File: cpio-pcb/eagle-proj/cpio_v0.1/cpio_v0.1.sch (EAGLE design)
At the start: 96 parts

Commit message: Schematic completed with GPIOS
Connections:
- net N$23 renamed GPIO13
- net N$36 renamed GPIO19
- net N$37 renamed GPIO26
- net N$60 renamed GPIO22
- net N$62 renamed GPIO5
- net N$63 renamed GPIO6
- net N$65 renamed GPIO17
- net N$66 renamed GPIO27
- removed net N$38: R_HSS_PROT_3.1
- removed net N$39: R_SS_PROT0.1
- removed net N$40: R_SS_PROT1.1
- removed net N$41: R_SS_PROT2.1
- removed net N$42: R_SS_PROT3.1
- net 3.3V: now also C_LDO3.3_2.1
- net 5V: now also C_LDO3.3_1.1
- net GPIO12: now also R_SS_PROT2.1
- net GPIO16: now also R_SS_PROT1.1
- net GPIO20: now also R_SS_PROT0.1
- net GPIO21: now also R_HSS_PROT_3.1
- net GPIO25: now also R_SS_PROT3.1
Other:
- note removed: "To which GPIOs?!"
- moved on the sheet: ADC, BEEP, CAMERA, C_ADC, C_LDO3.3_1, C_LDO3.3_2, C_RL_0, C_RL_1, C_RL_10, C_RL_11, C_RL_2, C_RL_3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

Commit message: First Review and modification of schematic
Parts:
- removed R_RGBLED: (no value), SparkFun-Passives:RESISTOR0805-RES
- removed R_SD_1A: 20k, SparkFun-Passives:RESISTOR0805-RES
- removed R_SD_2B: 9.1k, SparkFun-Passives:RESISTOR0805-RES
- removed R_SPI_0, R_SPI_1, R_SPI_2: 10k, SparkFun-Passives:RESISTOR0805-RES
- added C_ADC_B, C_ADC_PH, C_CUR_FILT, C_LVL, C_MUX, C_RL_12, C_SW, C_U_FILT: 100n, SparkFun-Passives:CAP0805
- added PUSH1: BUTTON, cpio:BUTTON
- added R_CM_LOAD1, R_CM_LOAD2: 100, SparkFun-Passives:RESISTOR0805-RES
- added R_PH: 10k, SparkFun-Passives:RESISTOR0805-RES
- added R_PUSHBUT1, R_PUSHBUT2: (no value), SparkFun-Passives:RESISTOR0805-RES
- added SENS_PH: XH-A-3, cpio:XH-A-3
- added U$2: DB2X41100L, cpio:DB2X41100L
- C_SD_3: value (none) -> 10n
- R_SD_1B: value 30k -> 82k
- R_SD_2A: value 430 -> 15k
- R_SD_EN: value 10M -> 10k
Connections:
- net GPIO27 renamed GPIO_XXXXX
- removed net ADC_PWR: ADC.AIN0, R_CM_LOAD.2, SENS_I.OUT
- removed net N$52: C_RL_10.1, C_RL_11.1, C_RL_8.1, C_RL_9.1, RL_BRIGHT.VDD, RL_CAMERA.VDD, RL_HUM_0.VDD, RL_HUM_1.VDD, R_RGBLED.1
- removed net N$61: C_RL_4.1, C_RL_5.1, C_RL_6.1, C_RL_7.1, RL_TEMP_0.VDD, RL_TEMP_1.VDD, RL_TEMP_2.VDD, RL_TEMP_3.VDD
- removed net N$67: C_RL_0.1, C_RL_1.1, C_RL_2.1, C_RL_3.1, RL_HEAT_0.VDD, RL_HEAT_1.VDD, RL_HEAT_2.VDD, RL_HEAT_3.VDD
- new net 3.3V1: C_MUX.2
- new net 3.3V2: C_SW.2
- new net 3.3V3: C_LVL.2
- new net ADC_CUR: ADC.AIN0, C_CUR_FILT.1, R_CM_LOAD.2, SENS_I.OUT
- new net ADC_PH: ADC.AIN3, C_ADC_PH.1, R_PH.1
- new net ADC_U: ADC.AIN1, C_U_FILT.1, R_CM_LOAD1.1, R_CM_LOAD2.2
- new net N$23: SWT_PWR.3, U$2.A
- new net N$7: R_PH.2, SENS_PH.1
- new net PI_3.3V: RP_HEAD.1, RP_HEAD.17
- net 12V: now also R_CM_LOAD1.2
- net 3.3V: now also R_PUSHBUT1.2; no longer RP_HEAD.1, RP_HEAD.17, R_SPI_0.2, R_SPI_1.2, R_SPI_2.2
- net 5V: now also C_RL_0.1, C_RL_1.1, C_RL_10.1, C_RL_11.1, C_RL_2.1, C_RL_3.1, C_RL_4.1, C_RL_5.1, C_RL_6.1, C_RL_7.1, C_RL_8.1, C_RL_9.1, RL_BRIGHT.VDD, RL_CAMERA.VDD, RL_HEAT_0.VDD, RL_HEAT_1.VDD, RL_HEAT_2.VDD, RL_HEAT_3.VDD, RL_HUM_0.VDD, RL_HUM_1.VDD, RL_TEMP_0.VDD, RL_TEMP_1.VDD, RL_TEMP_2.VDD, RL_TEMP_3.VDD; no longer R_RGBLED.2
- net ADC_BRIGHT: now also ADC.AIN2, C_ADC_B.1; no longer ADC.AIN1
- net GND: now also C_ADC_B.2, C_ADC_PH.2, C_LVL.1, C_MUX.1, C_RL_12.2, C_SW.1, C_U_FILT.2, PUSH1.P$1, R_CM_LOAD2.1
- net N$12: no longer R_SD_1A.1, R_SD_2B.2
- net N$13: no longer R_SD_2B.1
- net N$24: now also R_CM_SENS.1, SENS_I.VIN+, U$2.C; no longer ADC.AIN2
- net N$25: now also C_RL_12.1, R_PUSHBUT2.1; no longer ADC.AIN3
- net N$5: now also PUSH1.P$2, R_PUSHBUT1.1, R_PUSHBUT2.2; no longer R_CM_SENS.1, SENS_I.VIN+, SWT_PWR.3
- net N$9: no longer R_SD_1A.2
- net SPI0_MISO: no longer R_SPI_1.1
- net SPI0_MOSI: no longer R_SPI_2.1
- net SPI0_SCLK: no longer R_SPI_0.1
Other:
- note added: "1.2A"
- note added: "300mA"
- note added: "5.17V"
- note added: "5V is used for supply of Pi only: Pi should have an internal supply for 3.3V etc."
- note added: "Check Circuit!!!!"
- note added: "Check Suitability of Diode"
- note added: "Comments Raffael -Removed PullUps from SPI -simpler resisitive divider for 5V supply. Precision is not required. -Added some decoupling caps -Removed R for RGB. connected the three supply nets to 5V -Disconnected Pi's 3.3V from our 3.3V -Added protection Diode at supply input. -> now we can remove the ground protection circuit of the switch IC -Maybe overkill to have cap for each led. Can put foo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"
- note added: "Pull UP Required?"
- note removed: "DeCap?!"
- note removed: "Plugs for potential pH Sensors missing!"
- moved on the sheet: C_SD_1, C_SD_2, LED_PWR_12V, PUSH, R_LED_12V, R_PUSHBUT, R_SD_2A, R_SD_EN, STP_DN, SWT_PWR

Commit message: schematic review: button and some R less
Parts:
- removed C_RL_1, C_RL_11, C_RL_3, C_RL_5, C_RL_7, C_RL_9: 100n, SparkFun-Passives:CAP0805
- removed PUSH: BUTTON, cpio:BUTTON
- removed R_PUSHBUT: (no value), SparkFun-Passives:RESISTOR0805-RES
- removed R_SS_PROT0, R_SS_PROT1, R_SS_PROT2, R_SS_PROT3: 1k, SparkFun-Passives:RESISTOR0805-RES
- removed SENS_BRIGHT: XH-A-2, cpio:XH-A-2
- added C_IO1: 100n, SparkFun-Passives:CAP0805
- added SENS_PH1: XH-A-3, cpio:XH-A-3
- renumbered R_LED_3.3V1 to R_BEP
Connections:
- removed net GPIO_XXXXX: PUSH.P$1
- removed net N$20: R_SS_PROT1.2, SWT_SENS.2OE
- removed net N$21: R_SS_PROT2.2, SWT_SENS.3OE
- removed net N$22: R_SS_PROT3.2, SWT_SENS.4OE
- removed net N$25: C_RL_12.1, R_PUSHBUT2.1
- removed net N$57: PUSH.P$2, R_PUSHBUT.1
- new net GPIO_27: C_RL_12.1, R_PUSHBUT1.1, R_PUSHBUT2.2
- net 3.3V: now also C_IO1.1, SENS_PH.1, SENS_PH1.1; no longer R_PUSHBUT.2
- net 5V: no longer C_RL_1.1, C_RL_11.1, C_RL_3.1, C_RL_5.1, C_RL_7.1, C_RL_9.1
- net GND: now also C_IO1.2, SENS_PH.3, SENS_PH1.3; no longer C_RL_1.2, C_RL_11.2, C_RL_3.2, C_RL_5.2, C_RL_7.2, C_RL_9.2, SENS_BRIGHT.2
- net GPIO12: now also SWT_SENS.3OE; no longer R_SS_PROT2.1
- net GPIO16: now also SWT_SENS.2OE; no longer R_SS_PROT1.1
- net GPIO20: now also SWT_SENS.1OE; no longer R_SS_PROT0.1
- net GPIO25: now also SWT_SENS.4OE; no longer R_SS_PROT3.1
- net N$14: now also RL_HUM_0.DI; no longer R_SS_PROT0.2, SWT_SENS.1OE
- net N$35: now also SENS_PH1.2; no longer SENS_BRIGHT.1
- net N$5: now also R_PUSHBUT2.1; no longer R_PUSHBUT1.1, R_PUSHBUT2.2
- net N$58: no longer RL_HUM_0.DI
- net N$7: now also SENS_PH.2; no longer SENS_PH.1
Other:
- note added: "Comments Raffael -Removed PullUps from SPI -simpler resisitive divider for 5V supply. Precision is not required. -Added some decoupling caps -Removed R for RGB. connected the three supply nets to 5V -Disconnected Pi's 3.3V from our 3.3V -Added protection Diode at supply input. -> now we can remove the ground protection circuit of the switch IC -Values of current measurement need to be adapted. Wh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"
- note removed: "Check Circuit!!!!"
- note removed: "Comments Raffael -Removed PullUps from SPI -simpler resisitive divider for 5V supply. Precision is not required. -Added some decoupling caps -Removed R for RGB. connected the three supply nets to 5V -Disconnected Pi's 3.3V from our 3.3V -Added protection Diode at supply input. -> now we can remove the ground protection circuit of the switch IC -Maybe overkill to have cap for each led. Can put foo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"
- moved on the sheet: C_ADC_B, C_RL_12, PUSH1, R_BRIGHT, R_PUSHBUT1, R_PUSHBUT2, SENS_PH

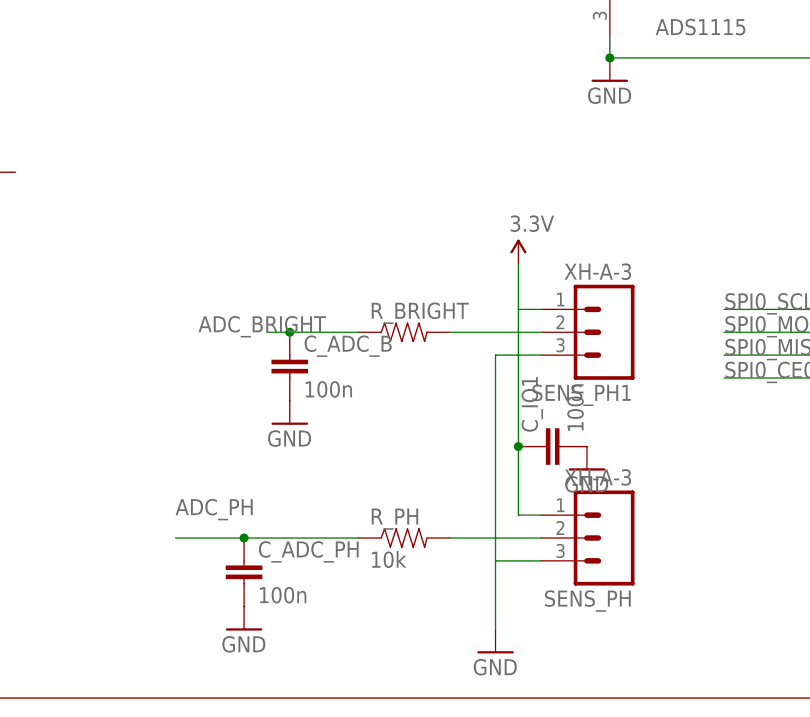
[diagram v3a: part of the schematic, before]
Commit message: rename brightness input. Now with gnd, signal, vcc
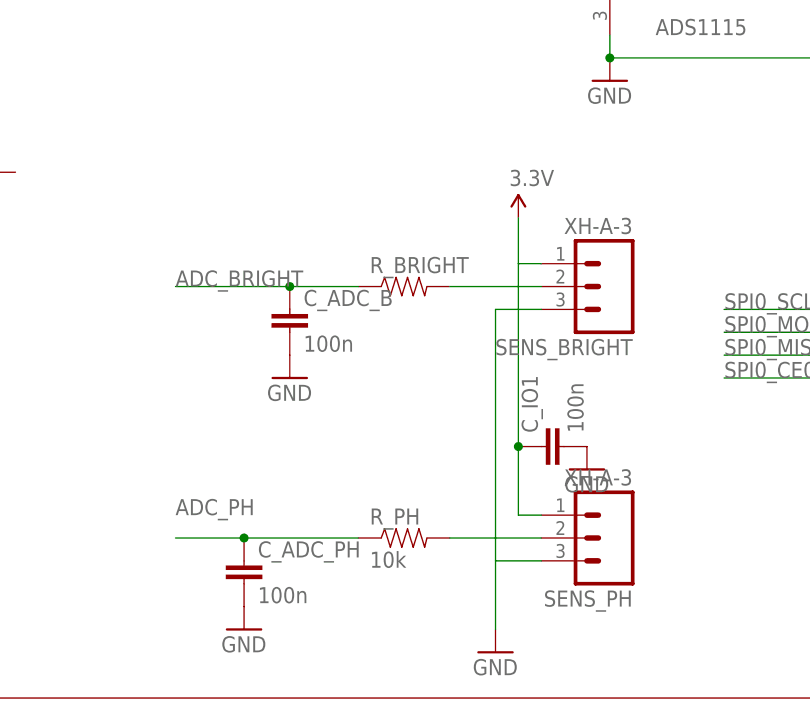
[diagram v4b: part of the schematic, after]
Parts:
- removed SENS_PH1: XH-A-3, cpio:XH-A-3
- added SENS_BRIGHT: XH-A-3, cpio:XH-A-3
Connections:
- net 3.3V: now also SENS_BRIGHT.1; no longer SENS_PH1.1
- net GND: now also SENS_BRIGHT.3; no longer SENS_PH1.3
- net N$35: now also SENS_BRIGHT.2; no longer SENS_PH1.2
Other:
- moved on the sheet: C_ADC_B, R_BRIGHT
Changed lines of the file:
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@@
 <part name="GND52" library="supply1" deviceset="GND" device=""/>
 <part name="SUPPLY7" library="SparkFun-Aesthetics" deviceset="3.3V" device=""/>
-<part name="SENS_PH1" library="cpio" deviceset="XH-A-3" device=""/>
+<part name="SENS_BRIGHT" library="cpio" deviceset="XH-A-3" device=""/>
 <part name="SUPPLY25" library="SparkFun-Aesthetics" deviceset="3.3V" device=""/>
 <part name="C_IO1" library="SparkFun-Passives" deviceset="CAP" device="0805" value="100n"/>
@@
 <instance part="R_HSS_PROT_3" gate="G$1" x="355.6" y="-30.48"/>
 <instance part="GND27" gate="1" x="355.6" y="-254"/>
-<instance part="R_BRIGHT" gate="G$1" x="345.44" y="-218.44"/>
+<instance part="R_BRIGHT" gate="G$1" x="345.44" y="-213.36"/>
 <instance part="CAMERA" gate="G$1" x="401.32" y="-218.44" rot="R180"/>
 <instance part="GND28" gate="1" x="393.7" y="-233.68"/>
@@
 <instance part="GND48" gate="1" x="251.46" y="-38.1"/>
 <instance part="SENS_PH" gate="G$1" x="368.3" y="-241.3" rot="R180"/>
-<instance part="C_ADC_B" gate="G$1" x="332.74" y="-223.52"/>
-<instance part="GND49" gate="1" x="332.74" y="-228.6"/>
+<instance part="C_ADC_B" gate="G$1" x="332.74" y="-218.44"/>
+<instance part="GND49" gate="1" x="332.74" y="-223.52"/>
 <instance part="GND50" gate="1" x="327.66" y="-251.46"/>
 <instance part="C_ADC_PH" gate="G$1" x="327.66" y="-246.38"/>
@@
 <instance part="GND52" gate="1" x="172.72" y="-251.46"/>
 <instance part="SUPPLY7" gate="G$1" x="172.72" y="-218.44"/>
-<instance part="SENS_PH1" gate="G$1" x="368.3" y="-218.44" rot="R180"/>
-<instance part="SUPPLY25" gate="G$1" x="358.14" y="-210.82"/>
+<instance part="SENS_BRIGHT" gate="G$1" x="368.3" y="-213.36" rot="R180"/>
+<instance part="SUPPLY25" gate="G$1" x="358.14" y="-205.74"/>
 <instance part="C_IO1" gate="G$1" x="363.22" y="-231.14" rot="R90"/>
 <instance part="GND53" gate="1" x="365.76" y="-233.68"/>
@@
 </segment>
 <segment>
-<wire x1="360.68" y1="-220.98" x2="355.6" y2="-220.98" width="0.1524" layer="91"/>
-<wire x1="355.6" y1="-220.98" x2="355.6" y2="-243.84" width="0.1524" layer="91"/>
+<wire x1="360.68" y1="-215.9" x2="355.6" y2="-215.9" width="0.1524" layer="91"/>
+<wire x1="355.6" y1="-215.9" x2="355.6" y2="-243.84" width="0.1524" layer="91"/>
 <pinref part="GND27" gate="1" pin="GND"/>
-<pinref part="SENS_PH1" gate="G$1" pin="3"/>
+<pinref part="SENS_BRIGHT" gate="G$1" pin="3"/>
 <pinref part="SENS_PH" gate="G$1" pin="3"/>
 <wire x1="355.6" y1="-243.84" x2="355.6" y2="-251.46" width="0.1524" layer="91"/>
@@
 <wire x1="360.68" y1="-238.76" x2="358.14" y2="-238.76" width="0.1524" layer="91"/>
 <wire x1="358.14" y1="-238.76" x2="358.14" y2="-231.14" width="0.1524" layer="91"/>
-<pinref part="SENS_PH1" gate="G$1" pin="1"/>
-<wire x1="358.14" y1="-231.14" x2="358.14" y2="-215.9" width="0.1524" layer="91"/>
-<wire x1="358.14" y1="-215.9" x2="358.14" y2="-210.82" width="0.1524" layer="91"/>
-<wire x1="360.68" y1="-215.9" x2="358.14" y2="-215.9" width="0.1524" layer="91"/>
+<pinref part="SENS_BRIGHT" gate="G$1" pin="1"/>
+<wire x1="358.14" y1="-231.14" x2="358.14" y2="-210.82" width="0.1524" layer="91"/>
+<wire x1="358.14" y1="-210.82" x2="358.14" y2="-205.74" width="0.1524" layer="91"/>
+<wire x1="360.68" y1="-210.82" x2="358.14" y2="-210.82" width="0.1524" layer="91"/>
 <pinref part="SUPPLY25" gate="G$1" pin="3.3V"/>
 <pinref part="C_IO1" gate="G$1" pin="1"/>
@@
 <segment>
 <pinref part="R_BRIGHT" gate="G$1" pin="2"/>
-<wire x1="360.68" y1="-218.44" x2="350.52" y2="-218.44" width="0.1524" layer="91"/>
-<pinref part="SENS_PH1" gate="G$1" pin="2"/>
+<wire x1="360.68" y1="-213.36" x2="350.52" y2="-213.36" width="0.1524" layer="91"/>
+<pinref part="SENS_BRIGHT" gate="G$1" pin="2"/>
 </segment>
 </net>
@@
 <segment>
 <pinref part="R_BRIGHT" gate="G$1" pin="1"/>
-<wire x1="340.36" y1="-218.44" x2="332.74" y2="-218.44" width="0.1524" layer="91"/>
-<label x="322.58" y="-218.44" size="1.778" layer="95"/>
+<wire x1="340.36" y1="-213.36" x2="332.74" y2="-213.36" width="0.1524" layer="91"/>
+<label x="320.04" y="-213.36" size="1.778" layer="95"/>
 <pinref part="C_ADC_B" gate="G$1" pin="1"/>
-<wire x1="332.74" y1="-218.44" x2="330.2" y2="-218.44" width="0.1524" layer="91"/>
-<junction x="332.74" y="-218.44"/>
-</segment>
-<segment>
+<wire x1="332.74" y1="-213.36" x2="320.04" y2="-213.36" width="0.1524" layer="91"/>
+<junction x="332.74" y="-213.36"/>
+</segment>
+<segment>

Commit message: clean up and deleting components
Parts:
- removed CAMERA: XH-A-6, cpio:XH-A-6
- removed C_RL_10, C_RL_4, C_RL_6, C_RL_8: 100n, SparkFun-Passives:CAP0805
- removed LED_0, LED_1, LED_2: (no value), SparkFun-LED:LED1206
- removed RL_BRIGHT, RL_CAMERA, RL_HUM_0, RL_HUM_1, RL_TEMP_0, RL_TEMP_1, RL_TEMP_2, RL_TEMP_3: WS2812B5050, adafruit:WS2812B5050
- removed R_LED_3.3V_0, R_LED_3.3V_1, R_LED_3.3V_2: (no value), SparkFun-Passives:RESISTOR0805-RES
- removed R_SPI_3: 10k, SparkFun-Passives:RESISTOR0805-RES
- added LED_RP: (no value), SparkFun-LED:LED1206
- added R_LED_RP: (no value), SparkFun-Passives:RESISTOR0805-RES
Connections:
- net GPIO_27 renamed GPIO27
- removed net GPIO22: LED_0.C
- removed net GPIO5: LED_1.C
- removed net GPIO6: LED_2.C
- removed net N$14: RL_HUM_0.DI
- removed net N$46: RL_TEMP_2.DO, RL_TEMP_3.DI
- removed net N$47: RL_TEMP_1.DO, RL_TEMP_2.DI
- removed net N$48: RL_TEMP_0.DO, RL_TEMP_1.DI
- removed net N$49: RL_BRIGHT.DO, RL_CAMERA.DI
- removed net N$50: RL_BRIGHT.DI, RL_HUM_1.DO
- removed net N$51: RL_HUM_0.DO, RL_HUM_1.DI
- removed net N$54: LED_0.A, R_LED_3.3V_0.1
- removed net N$55: LED_1.A, R_LED_3.3V_1.1
- removed net N$56: LED_2.A, R_LED_3.3V_2.1
- removed net N$58: RL_TEMP_3.DO
- removed net N$59: RL_HEAT_3.DO, RL_TEMP_0.DI
- removed net SPI0_MISO: CAMERA.4
- removed net SPI0_MOSI: CAMERA.3
- removed net SPI0_SCLK: CAMERA.2
- new net N$20: LED_RP.A, R_LED_RP.1
- net 3.3V: no longer CAMERA.1, R_LED_3.3V_0.2, R_LED_3.3V_1.2, R_LED_3.3V_2.2, R_SPI_3.2
- net 5V: no longer C_RL_10.1, C_RL_4.1, C_RL_6.1, C_RL_8.1, RL_BRIGHT.VDD, RL_CAMERA.VDD, RL_HUM_0.VDD, RL_HUM_1.VDD, RL_TEMP_0.VDD, RL_TEMP_1.VDD, RL_TEMP_2.VDD, RL_TEMP_3.VDD
- net GND: now also LED_RP.C; no longer CAMERA.6, C_RL_10.2, C_RL_4.2, C_RL_6.2, C_RL_8.2, RL_BRIGHT.GND, RL_CAMERA.GND, RL_HUM_0.GND, RL_HUM_1.GND, RL_TEMP_0.GND, RL_TEMP_1.GND, RL_TEMP_2.GND, RL_TEMP_3.GND
- net PI_3.3V: now also R_LED_RP.2
- net SPI0_CE0_N: no longer CAMERA.5, R_SPI_3.1
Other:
- moved on the sheet: ADC, BEEP, C_ADC, C_ADC_B, C_ADC_PH, C_IO1, C_LDO3.3_1, C_LDO3.3_2, C_RL_12, C_SD_1, C_SD_2, C_SD_3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

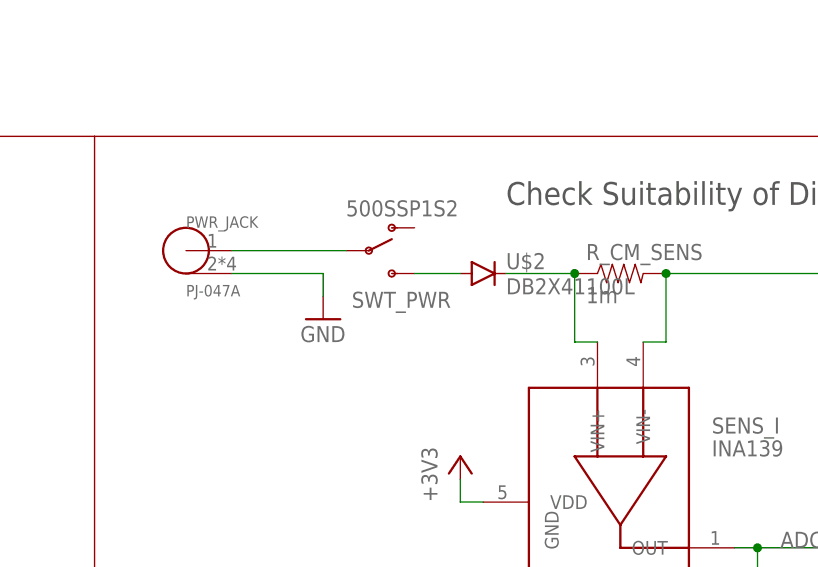
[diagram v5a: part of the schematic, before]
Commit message: Second Scetch of PCB layout with removed components
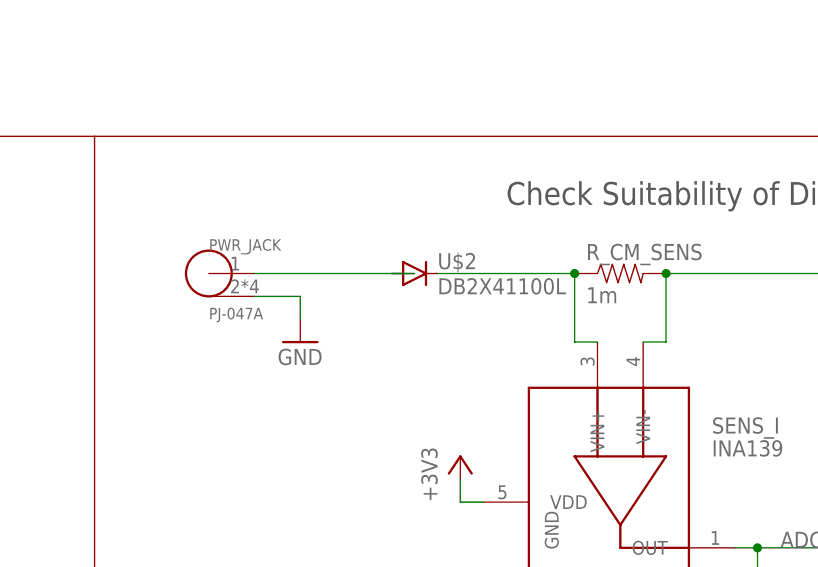
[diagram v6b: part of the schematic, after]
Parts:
- removed SWT_PWR: 500SSP1S2, cpio:500SSP1S2
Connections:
- net N$23: no longer SWT_PWR.3
- net N$3: no longer SWT_PWR.2
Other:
- moved on the sheet: PWR_JACK, U$2
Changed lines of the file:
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@@
 <part name="GND12" library="supply1" deviceset="GND" device=""/>
 <part name="SUPPLY1" library="SparkFun-Aesthetics" deviceset="12V" device=""/>
-<part name="SWT_PWR" library="cpio" deviceset="500SSP1S2" device=""/>
 <part name="SUPPLY2" library="SparkFun-Aesthetics" deviceset="12V" device=""/>
 <part name="C_SD_1" library="SparkFun-Passives" deviceset="CAP" device="0805" value="4.7u"/>
@@
 <instance part="GND8" gate="1" x="53.34" y="-76.2"/>
 <instance part="RP_HEAD" gate="G$1" x="86.36" y="-48.26"/>
-<instance part="PWR_JACK" gate="G$1" x="170.18" y="-12.7"/>
-<instance part="GND9" gate="1" x="185.42" y="-20.32"/>
+<instance part="PWR_JACK" gate="G$1" x="172.72" y="-15.24"/>
+<instance part="GND9" gate="1" x="182.88" y="-22.86"/>
 <instance part="LED_PWR_12V" gate="G$1" x="274.32" y="-40.64"/>
 <instance part="SENS_I" gate="G$1" x="218.44" y="-38.1"/>
@@
 <instance part="GND12" gate="1" x="233.68" y="-68.58"/>
 <instance part="SUPPLY1" gate="G$1" x="398.78" y="-15.24"/>
-<instance part="SWT_PWR" gate="G$1" x="190.5" y="-12.7"/>
 <instance part="SUPPLY2" gate="G$1" x="167.64" y="-119.38"/>
 <instance part="C_SD_1" gate="G$1" x="167.64" y="-127"/>
@@
 <instance part="SUPPLY24" gate="G$1" x="40.64" y="-154.94"/>
 <instance part="SUPPLY6" gate="G$1" x="38.1" y="-15.24"/>
-<instance part="U$2" gate="G$1" x="203.2" y="-15.24"/>
+<instance part="U$2" gate="G$1" x="195.58" y="-15.24"/>
 <instance part="R_PUSHBUT1" gate="G$1" x="119.38" y="-111.76" rot="R90"/>
 <instance part="PUSH1" gate="G$1" x="119.38" y="-142.24" rot="R90"/>
@@
 <pinref part="PWR_JACK" gate="G$1" pin="GND"/>
 <pinref part="GND9" gate="1" pin="GND"/>
-<wire x1="175.26" y1="-15.24" x2="185.42" y2="-15.24" width="0.1524" layer="91"/>
-<wire x1="185.42" y1="-15.24" x2="185.42" y2="-17.78" width="0.1524" layer="91"/>
+<wire x1="177.8" y1="-17.78" x2="182.88" y2="-17.78" width="0.1524" layer="91"/>
+<wire x1="182.88" y1="-17.78" x2="182.88" y2="-20.32" width="0.1524" layer="91"/>
 </segment>
 <segment>
@@
 <net name="N$3" class="0">
 <segment>
-<pinref part="SWT_PWR" gate="G$1" pin="2"/>
 <pinref part="PWR_JACK" gate="G$1" pin="PWR"/>
-<wire x1="187.96" y1="-12.7" x2="175.26" y2="-12.7" width="0.1524" layer="91"/>
+<wire x1="195.58" y1="-15.24" x2="177.8" y2="-15.24" width="0.1524" layer="91"/>
 </segment>
 </net>
@@
 <net name="N$23" class="0">
 <segment>
-<pinref part="SWT_PWR" gate="G$1" pin="3"/>
 <pinref part="U$2" gate="G$1" pin="A"/>
-<wire x1="200.66" y1="-15.24" x2="195.58" y2="-15.24" width="0.1524" layer="91"/>
+<wire x1="193.04" y1="-15.24" x2="195.58" y2="-15.24" width="0.1524" layer="91"/>
 </segment>
 </net>
@@
 <pinref part="R_CM_SENS" gate="G$1" pin="1"/>
 <pinref part="U$2" gate="G$1" pin="C"/>
-<wire x1="205.74" y1="-15.24" x2="213.36" y2="-15.24" width="0.1524" layer="91"/>
+<wire x1="198.12" y1="-15.24" x2="213.36" y2="-15.24" width="0.1524" layer="91"/>
 <wire x1="213.36" y1="-22.86" x2="213.36" y2="-15.24" width="0.1524" layer="91"/>
 <junction x="213.36" y="-15.24"/>
